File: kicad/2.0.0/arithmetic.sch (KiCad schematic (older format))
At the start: 70 parts

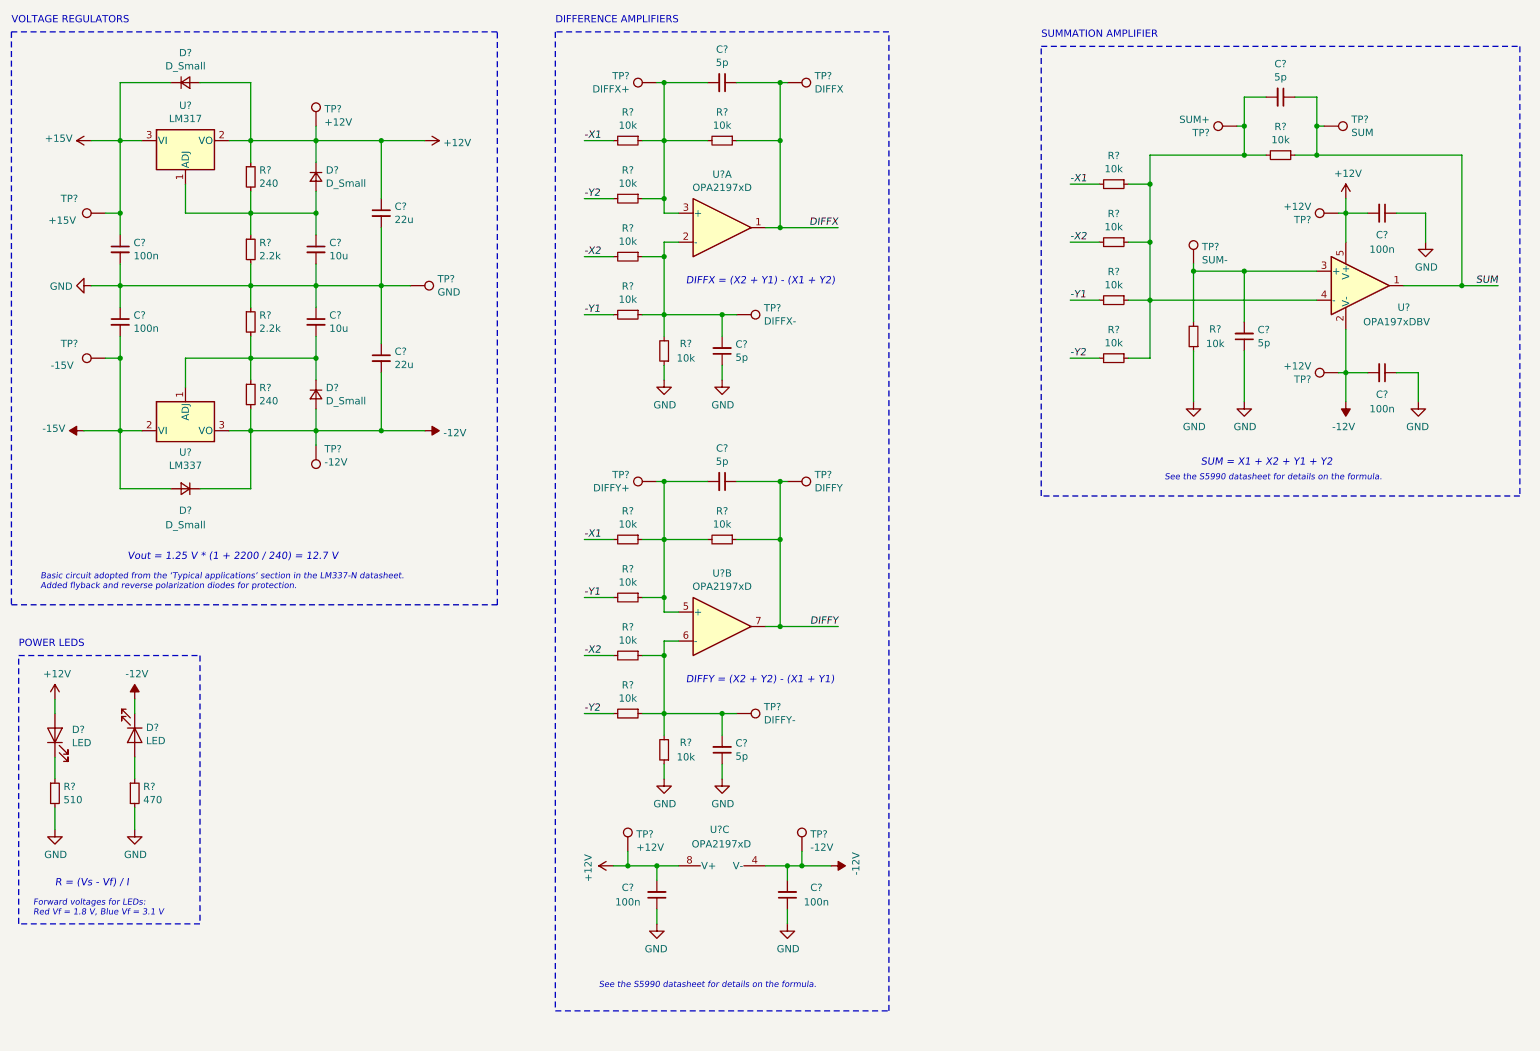
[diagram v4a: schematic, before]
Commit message: completed arithmetic 2.0.0 schematic, associated footprints
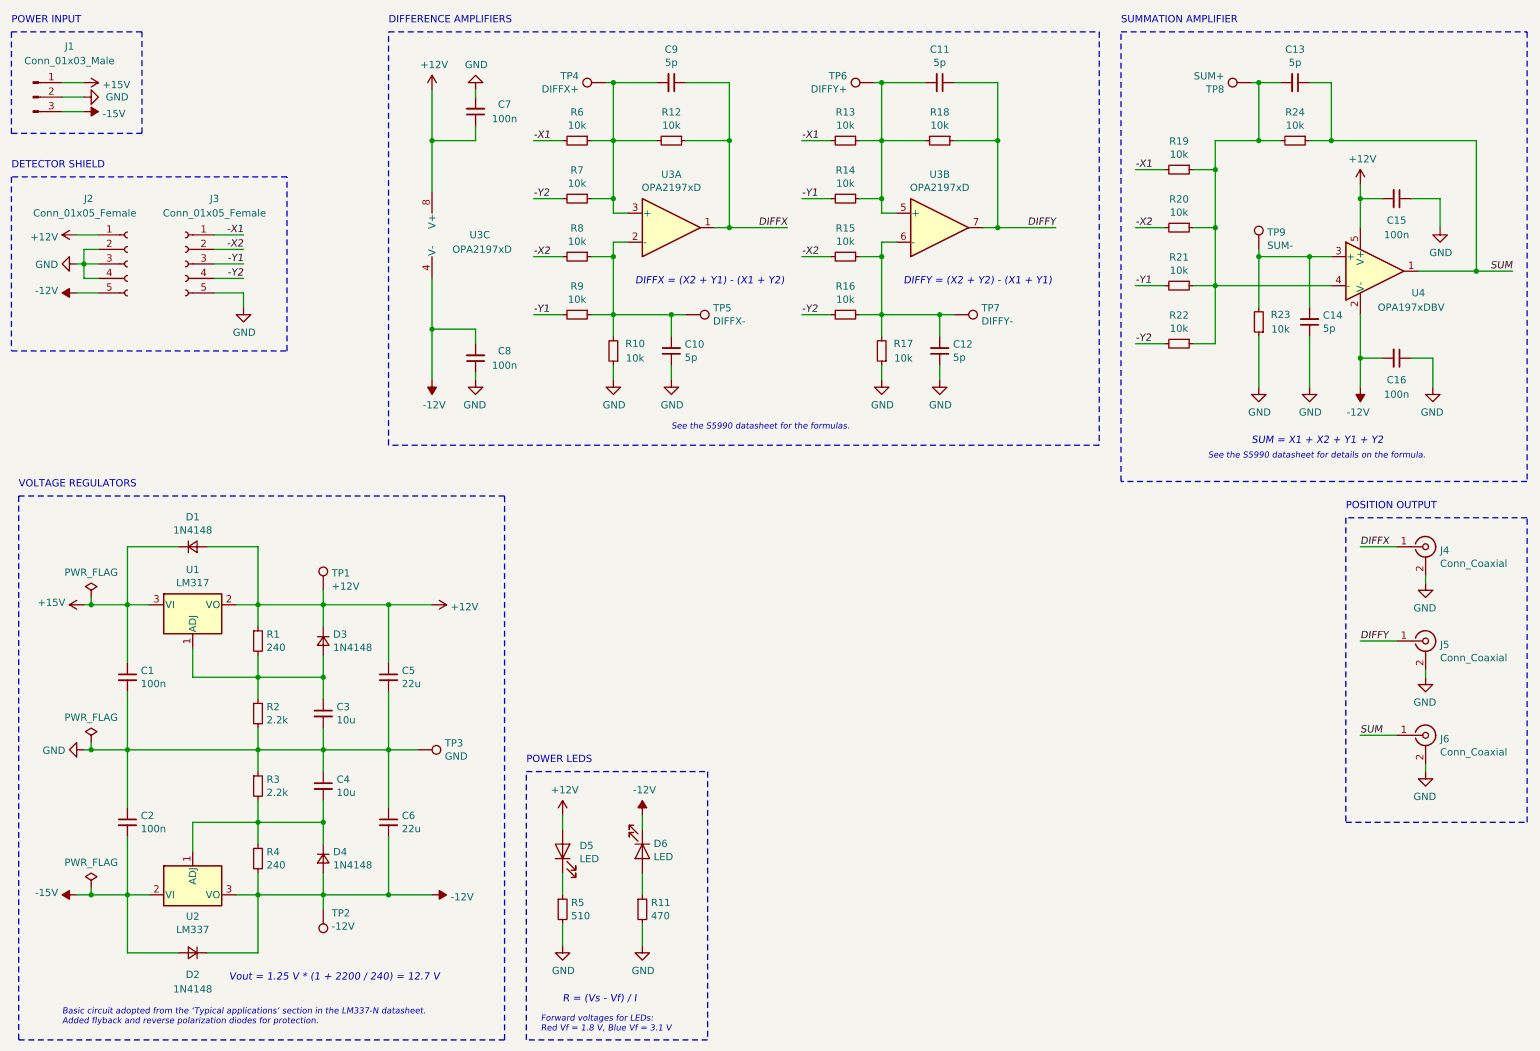
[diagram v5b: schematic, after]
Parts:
- removed TP? (x3): +12V, symbol Connector:TestPoint
- removed TP?: -12V, symbol Connector:TestPoint
- removed TP?: -15V, symbol Connector:TestPoint
- removed TP?: SUM, symbol Connector:TestPoint
- removed TP?: +15V, symbol Connector:TestPoint
- removed TP?: DIFFX, symbol Connector:TestPoint
- removed TP?: DIFFY, symbol Connector:TestPoint
- added J1: Conn_01x03_Male, Connector:FanPinHeader_1x03_P2.54mm_Vertical, symbol Connector:Conn_01x03_Male
- added J2, J3: Conn_01x05_Female, Connector_PinSocket_2.54mm:PinSocket_1x05_P2.54mm_Vertical, symbol Connector:Conn_01x05_Female
- added J4, J5, J6: Conn_Coaxial, Common:SMA_Molex_73251-2120_EdgeMount, symbol Connector:Conn_Coaxial
- C10, C11, C12, C13, C14, C9: renamed from C?; footprint (none) -> Capacitor_SMD:C_0603_1608Metric
- D1, D2, D3, D4: renamed from D?; value D_Small -> 1N4148; footprint (none) -> Diode_SMD:D_SOD-123
- D5, D6: renamed from D?; footprint (none) -> LED_SMD:LED_0603_1608Metric
- R11, R5: renamed from R?; footprint (none) -> Resistor_SMD:R_0603_1608Metric
- TP1, TP2, TP3, TP4, TP5, TP6, TP7, TP8, TP9: renamed from TP?; footprint (none) -> TestPoint:TestPoint_Pad_D1.0mm
- gave numbers to parts that had none: 36
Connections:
- net +12V: now also C7.1, J2.1 (Pin_1); no longer C8.2
- net +15V: now also J1.1 (Pin_1)
- net -12V: now also C8.2, J2.5 (Pin_5); no longer C7.2
- net -15V: now also J1.3 (Pin_3)
- net -X1: now also J3.1 (Pin_1)
- net -X2: now also J3.2 (Pin_2)
- net -Y1: now also J3.3 (Pin_3)
- net -Y2: now also J3.4 (Pin_4)
- net DIFFX: now also J4.1 (In)
- net DIFFY: now also J5.1 (In)
- net GND: now also C7.2, J1.2 (Pin_2), J2.2 (Pin_2), J2.3 (Pin_3), J2.4 (Pin_4), J3.5 (Pin_5), J4.2 (Ext), J5.2 (Ext), J6.2 (Ext); no longer C7.1
- net SUM: now also J6.1 (In)
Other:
- note added: "DETECTOR SHIELD"
- note added: "POSITION OUTPUT"
- note added: "POWER INPUT"
- note added: "See the S5990 datasheet for the formulas."
- moved on the sheet: C1, C10, C11, C12, C13, C14, C15, C16, C2, C3, C4, C5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

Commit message: added first attempt for the 2.0.0 arithmetic pcb design
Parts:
- C3, C4: footprint Capacitor_SMD:C_1206_3216Metric -> Capacitor_SMD:C_1210_3225Metric
- C5, C6: footprint Capacitor_SMD:C_0603_1608Metric -> Capacitor_SMD:C_1210_3225Metric
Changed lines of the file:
@@
 F 0 "C6" H 3292 6246 50  0000 L CNN
 F 1 "22u" H 3292 6155 50  0000 L CNN
-F 2 "Capacitor_SMD:C_0603_1608Metric" H 3200 6200 50  0001 C CNN
+F 2 "Capacitor_SMD:C_1210_3225Metric" H 3200 6200 50  0001 C CNN
 F 3 "~" H 3200 6200 50  0001 C CNN
 	1    3200 6200
@@
 F 0 "C4" H 2842 5996 50  0000 L CNN
 F 1 "10u" H 2842 5905 50  0000 L CNN
-F 2 "Capacitor_SMD:C_1206_3216Metric" H 2750 5950 50  0001 C CNN
+F 2 "Capacitor_SMD:C_1210_3225Metric" H 2750 5950 50  0001 C CNN
 F 3 "~" H 2750 5950 50  0001 C CNN
 	1    2750 5950
@@
 F 0 "C5" H 3292 5246 50  0000 L CNN
 F 1 "22u" H 3292 5155 50  0000 L CNN
-F 2 "Capacitor_SMD:C_0603_1608Metric" H 3200 5200 50  0001 C CNN
+F 2 "Capacitor_SMD:C_1210_3225Metric" H 3200 5200 50  0001 C CNN
 F 3 "~" H 3200 5200 50  0001 C CNN
 	1    3200 5200
@@
 F 0 "C3" H 2842 5496 50  0000 L CNN
 F 1 "10u" H 2842 5405 50  0000 L CNN
-F 2 "Capacitor_SMD:C_1206_3216Metric" H 2750 5450 50  0001 C CNN
+F 2 "Capacitor_SMD:C_1210_3225Metric" H 2750 5450 50  0001 C CNN
 F 3 "~" H 2750 5450 50  0001 C CNN
 	1    2750 5450

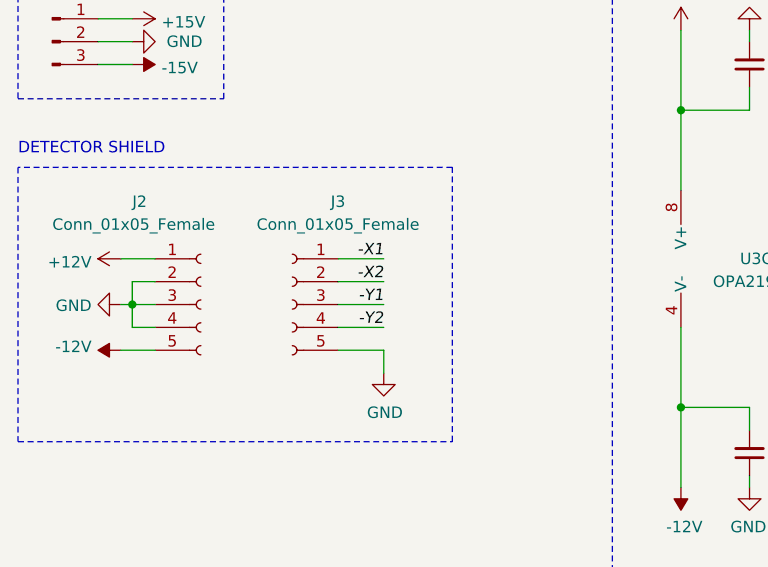
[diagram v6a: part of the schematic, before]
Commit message: routed traces for 2.0.0 pcbs
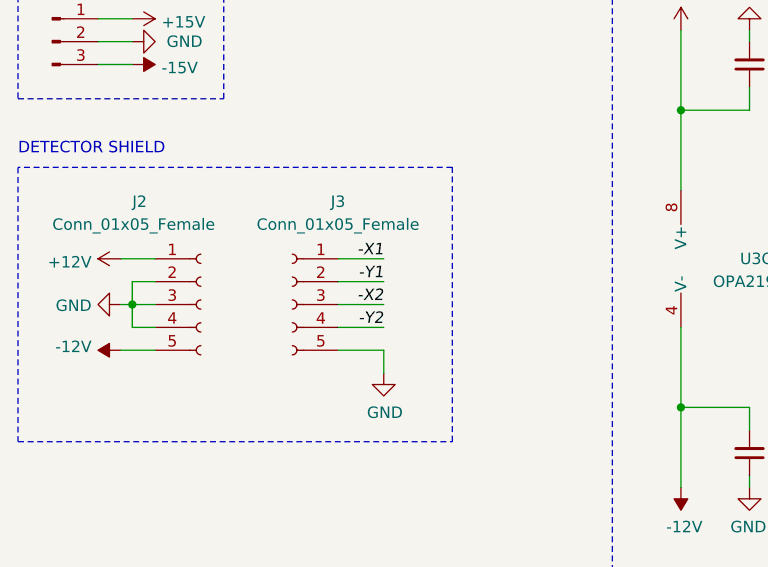
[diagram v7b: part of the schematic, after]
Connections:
- net -X2: now also J3.3 (Pin_3); no longer J3.2 (Pin_2)
- net -Y1: now also J3.2 (Pin_2); no longer J3.3 (Pin_3)
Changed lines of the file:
@@
 Text Label 2200 2150 2    50   Italic 0
 -X1
+Text Label 2200 2350 2    50   Italic 0
+-X2
 Text Label 2200 2250 2    50   Italic 0
--X2
-Text Label 2200 2350 2    50   Italic 0
 -Y1
 Text Label 2200 2450 2    50   Italic 0

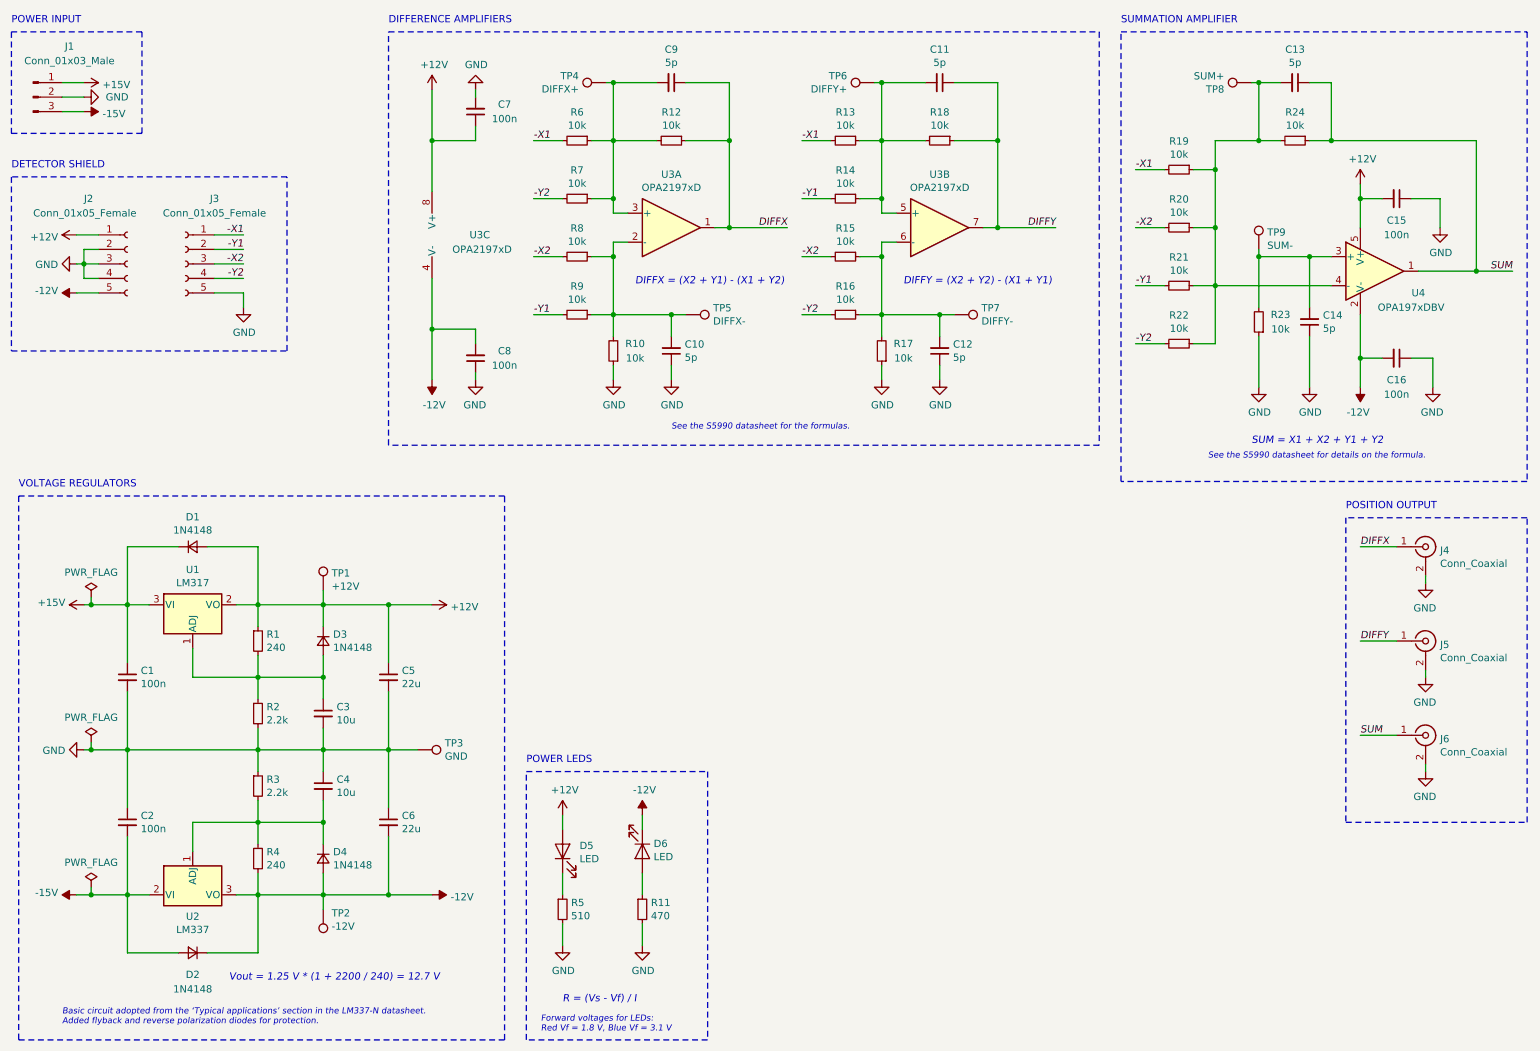
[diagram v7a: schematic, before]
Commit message: replaced dual op-amp on 2.0.0 arithmetic board with two op-amps
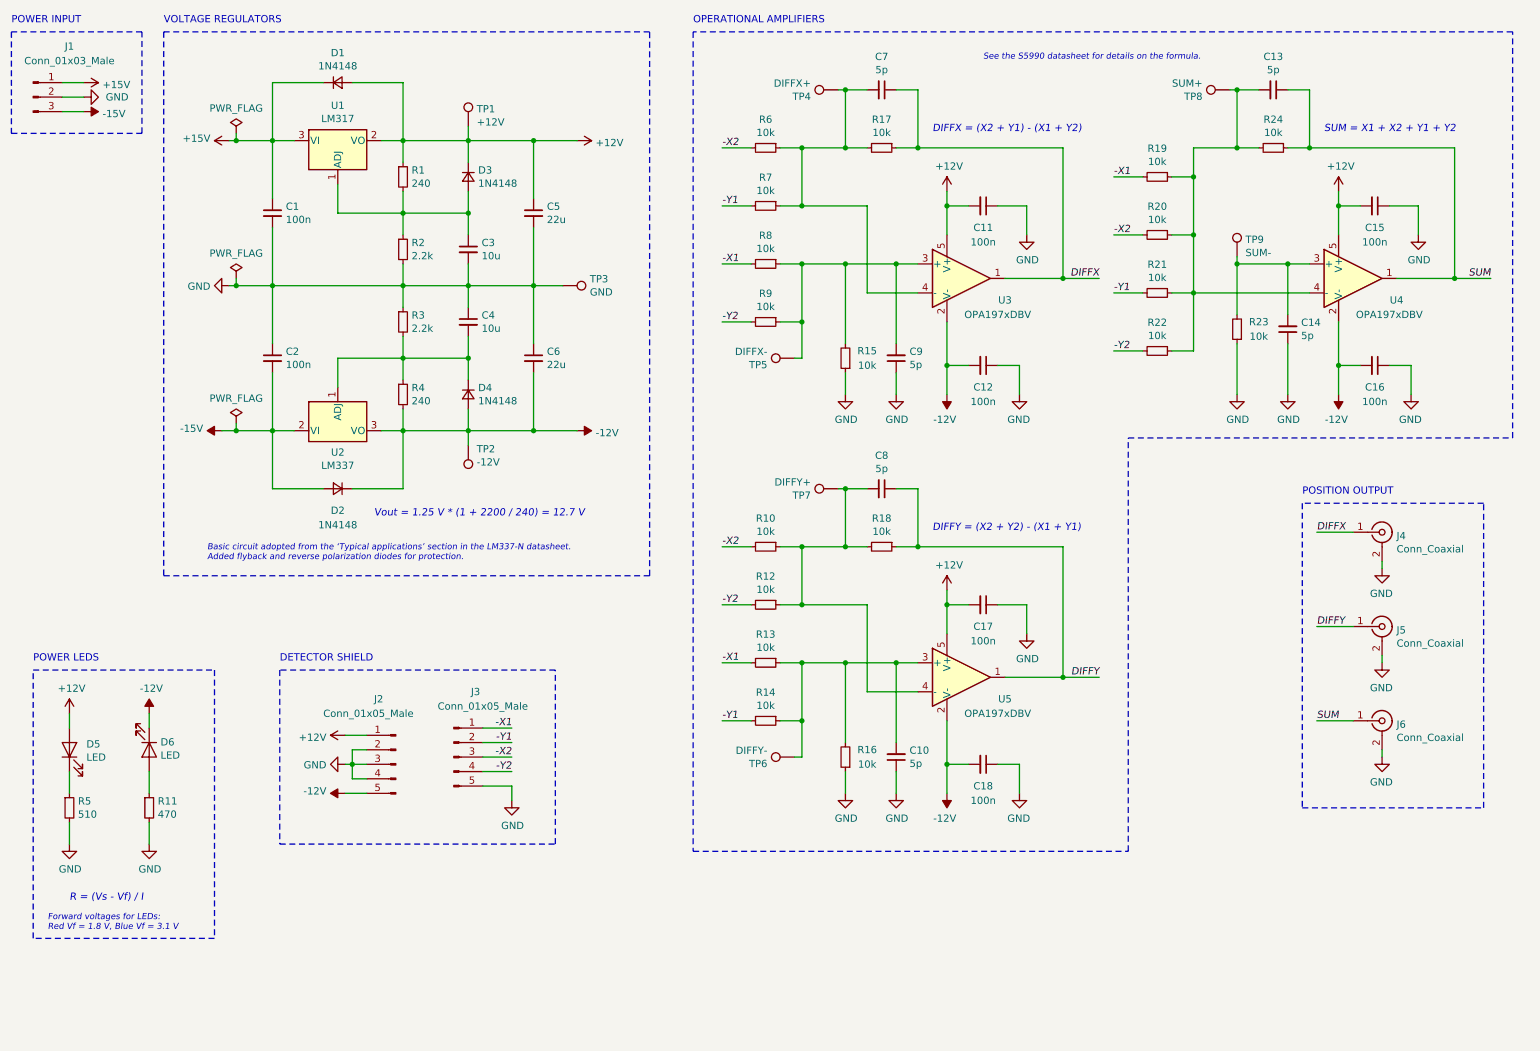
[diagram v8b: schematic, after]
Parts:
- removed J2, J3: Conn_01x05_Female, Connector_PinSocket_2.54mm:PinSocket_1x05_P2.54mm_Vertical, symbol Connector:Conn_01x05_Female
- removed U3: OPA2197xD, Package_SO:SOIC-8_3.9x4.9mm_P1.27mm, symbol Amplifier_Operational:OPA2197xD
- added C17, C18: 100n, Capacitor_SMD:C_0603_1608Metric, symbol Device:C_Small
- added J2, J3: Conn_01x05_Male, Connector_PinHeader_2.54mm:PinHeader_1x05_P2.54mm_Vertical, symbol Connector:Conn_01x05_Male
- added U3, U5: OPA197xDBV, Package_SO:SOIC-8_3.9x4.9mm_P1.27mm, symbol Amplifier_Operational:OPA197xDBV
- C11, C12: value 5p -> 100n
- C7, C8: value 100n -> 5p
- TP6: value DIFFY+ -> DIFFY-
- TP7: value DIFFY- -> DIFFY+
- U4: footprint Package_TO_SOT_SMD:SOT-23-5 -> Package_SO:SOIC-8_3.9x4.9mm_P1.27mm
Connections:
- net +12V: now also C11.2, C17.2, J2.1 (Pin_1), U3.5 (V+), U5.5 (V+); no longer C7.1
- net -12V: now also C12.2, C18.2, J2.5 (Pin_5), U3.2 (V-), U5.2 (V-); no longer C8.2
- net -X1: now also R8.2, J3.1 (Pin_1); no longer R6.2
- net -X2: now also R10.2, R6.2, J3.3 (Pin_3); no longer R15.2, R8.2
- net -Y1: now also R7.2, J3.2 (Pin_2); no longer R9.2
- net -Y2: now also R12.2, R9.2, J3.4 (Pin_4); no longer R16.2, R7.2
- net DIFFX: now also C7.1, R17.1, U3.1; no longer C9.1, R12.1
- net DIFFY: now also C8.1, U5.1; no longer C11.1
- net GND: now also C11.1, C9.1, R15.1, R16.1, C17.1, C18.1, J2.2 (Pin_2), J2.3 (Pin_3), J2.4 (Pin_4), J3.5 (Pin_5); no longer C7.2, C8.1, R10.1, R17.1
- net at R8.1, R9.1, TP5.1: now also C9.2, R15.2, U3.3 (+); no longer C10.2, R10.2
- net at R6.1, R7.1, TP4.1: now also C7.2, R17.2, U3.4 (-); no longer C9.2, R12.2
- net at R13.1, R14.1, TP6.1: now also C10.2, R16.2, U5.3 (+); no longer C11.2, R18.2
- new net: C8.2, R10.1, R12.1, R18.2, TP7.1, U5.4 (-)
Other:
- note added: "OPERATIONAL AMPLIFIERS"
- note removed: "DIFFERENCE AMPLIFIERS"
- note removed: "SUMMATION AMPLIFIER"
- note removed: "See the S5990 datasheet for the formulas."
- moved on the sheet: C1, C13, C14, C15, C16, C2, C3, C4, C5, C6, D1, D2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
